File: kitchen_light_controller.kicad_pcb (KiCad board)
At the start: 2 copper layers, 48 x 57 mm, 10 parts, among them J1 1935161, J2 1935161, J3 1935161, U1 SC0915, U2 VND7140AJTR

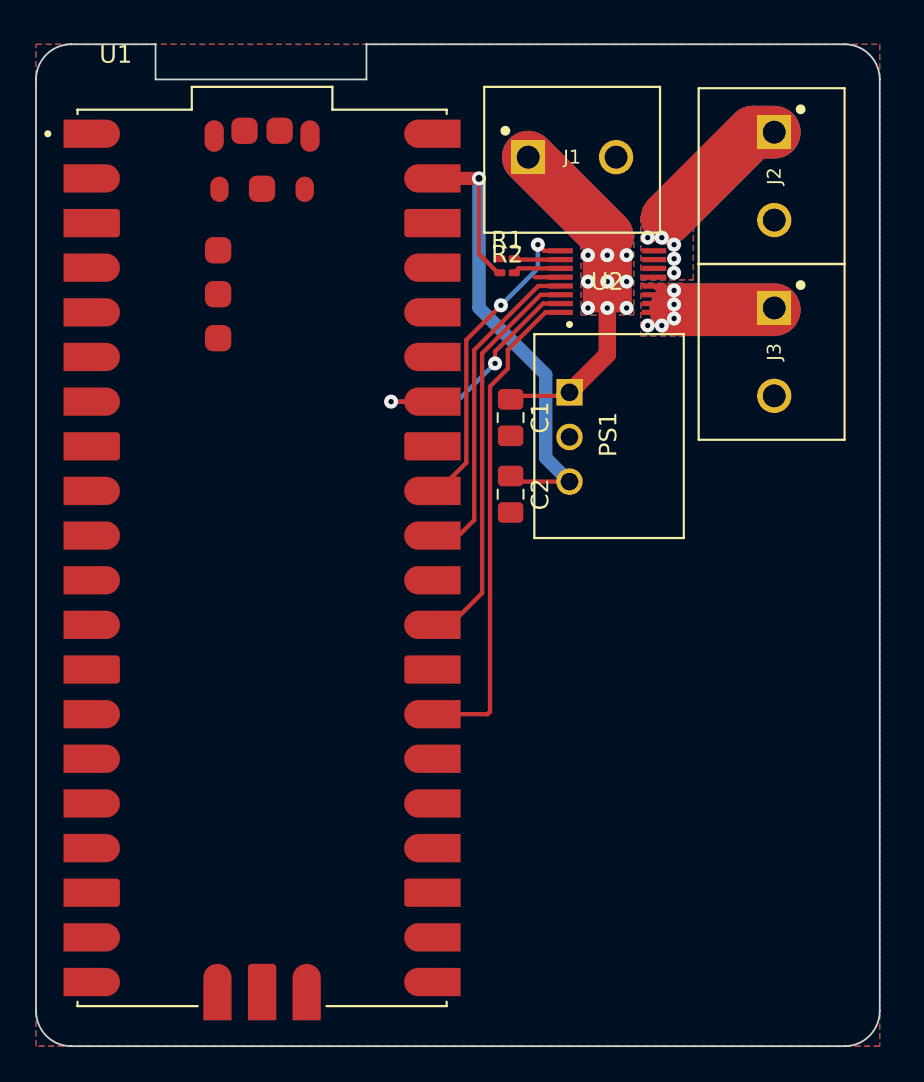
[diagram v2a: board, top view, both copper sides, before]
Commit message: Added debounced control switches
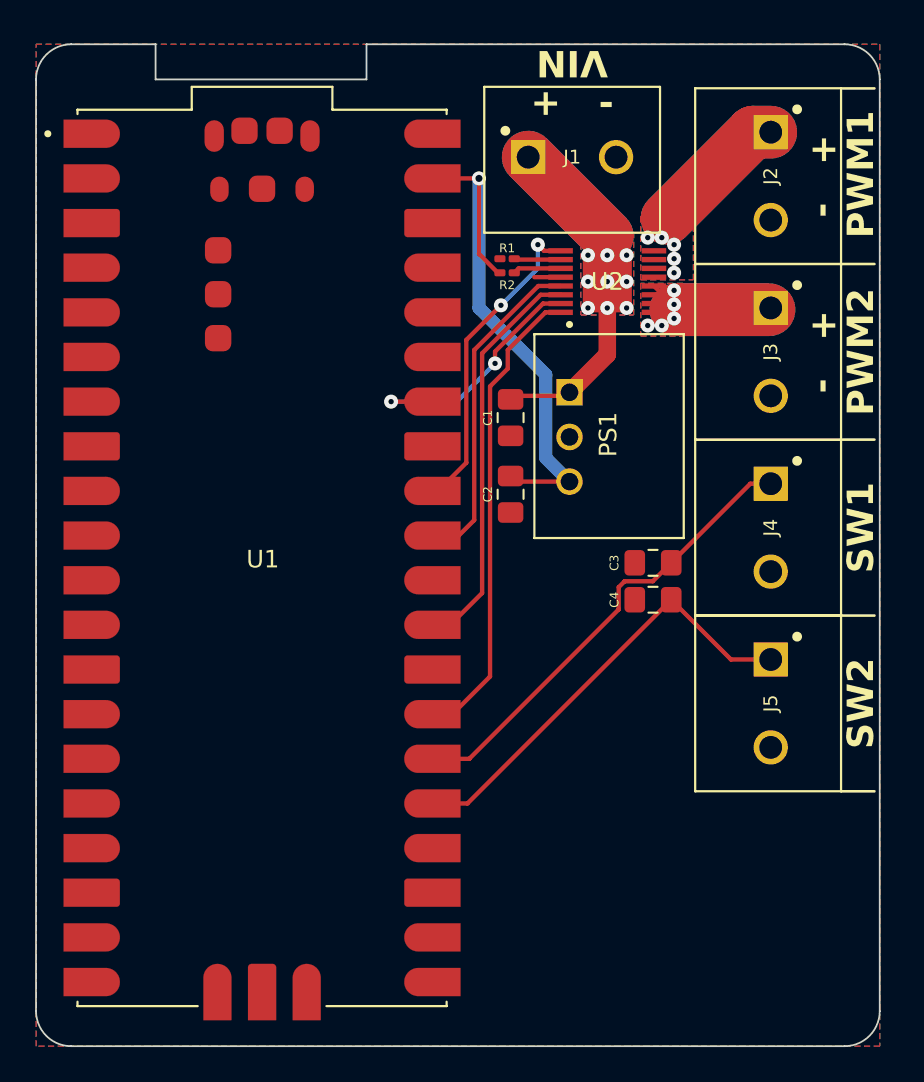
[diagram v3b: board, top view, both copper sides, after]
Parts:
- added C3: 1μF, Capacitor_SMD:C_0805_2012Metric_Pad1.18x1.45mm_HandSolder, F.Cu at (111.1, 58.5)
- added C4: 1μF, Capacitor_SMD:C_0805_2012Metric_Pad1.18x1.45mm_HandSolder, F.Cu at (111.1, 60.6)
- added J4: 1935161, Raspberry Pi Pico:PHOENIX_1935161, F.Cu at (117.8, 56.5)
- added J5: 1935161, Raspberry Pi Pico:PHOENIX_1935161, F.Cu at (117.8, 66.5)
- moved J2 0.20 mm to (117.8, 36.5)
- moved J3 0.20 mm to (117.8, 46.5)
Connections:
- U1 pad 13: Net-(U1-GND-Pad13) -> GND
- U1 pad 18: Net-(U1-GND-Pad13) -> GND
- U1 pad 23: Net-(U1-GND-Pad13) -> GND
- U1 pad 25: unconnected-(U1-GP19-Pad25) -> SW2
- U1 pad 26: unconnected-(U1-GP20-Pad26) -> SW1
- U1 pad 28: Net-(U1-GND-Pad13) -> GND
- U1 pad 3: Net-(U1-GND-Pad13) -> GND
- U1 pad 38: Net-(U1-GND-Pad13) -> GND
- U1 pad 8: Net-(U1-GND-Pad13) -> GND
- U1 pad D2: Net-(U1-GND-Pad13) -> GND
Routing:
- net SW1: track 0.00 -> 26.5 mm
- net SW2: track 0.00 -> 25.5 mm
- net 3.3V: track 34.1 -> 31.5 mm
- net PWM1: track 28.2 -> 27.1 mm
- net Net-(J3-Pad1): track 13.0 -> 12.4 mm
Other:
- board text added: "+ -"
- board text added: "PWM1"
- board text added: "PWM2"
- board text added: "SW1"
- board text added: "SW2"
- board text added: "VIN"

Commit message: Added analog motion sensor header
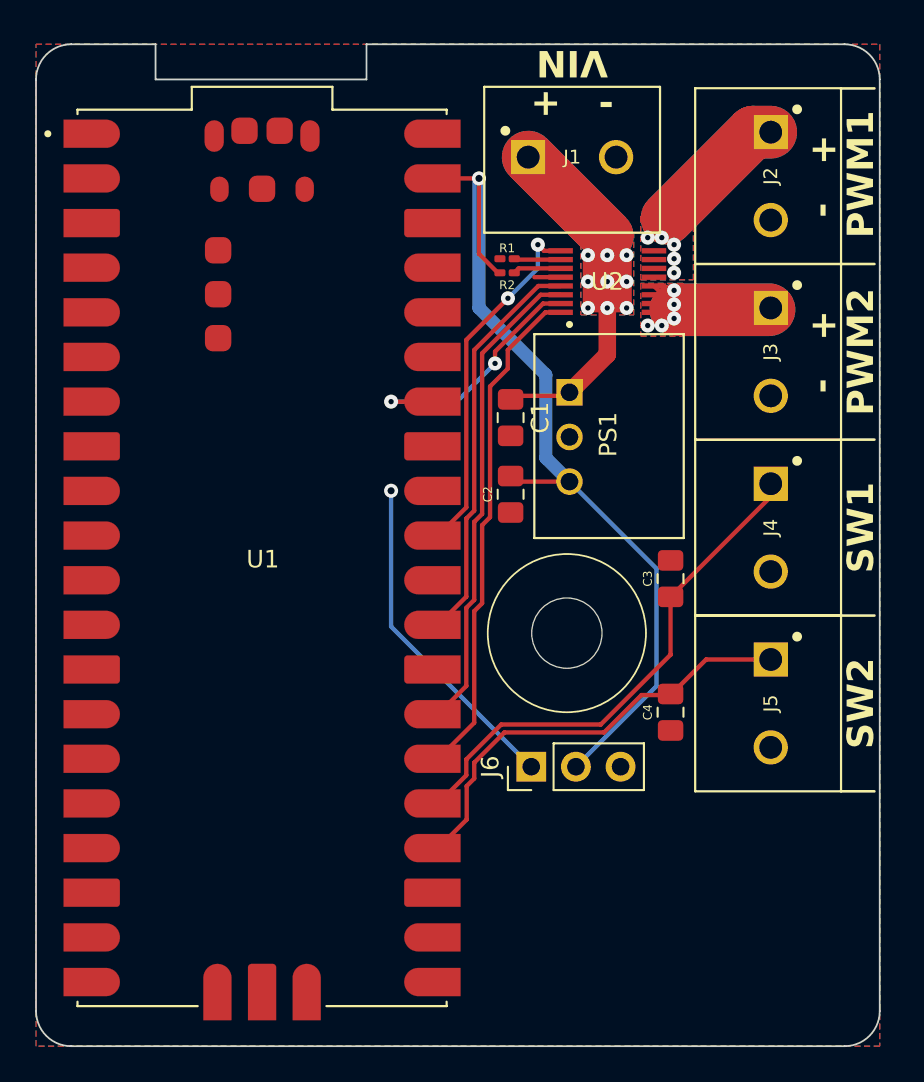
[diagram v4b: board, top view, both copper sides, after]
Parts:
- added J6: Conn_01x03, Connector_PinHeader_2.54mm:PinHeader_1x03_P2.54mm_Vertical, F.Cu at (104.2, 70.1)
- added REF**: MountingHole_Custom, kitchen_light_controller_parts:MountingHole_Custom, F.Cu at (106.2, 62.5)
- moved C4 6.48 mm to (112.1, 67.0), turned to 90 degrees
- moved C3 1.35 mm to (112.1, 59.4), turned to -90 degrees
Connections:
- U1 pad 24: unconnected-(U1-GP18-Pad24) -> SW2
- U1 pad 25: SW2 -> SW1
- U1 pad 26: SW1 -> PWM1
- U1 pad 27: PWM1 -> MS_SEL1
- U1 pad 29: MS_SEL1 -> MS_SEL0
- U1 pad 31: MS_SEL0 -> PWM0
- U1 pad 32: PWM0 -> MOTION_SIGNAL
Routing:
- net 3.3V: track 31.5 -> 51.7 mm
- net MOTION_SIGNAL: track 0.00 -> 19.3 mm, vias 0 -> 1
- net MS_SEL1: track 23.1 -> 28.9 mm
- net MS_SEL0: track 18.8 -> 23.8 mm
- net SW1: track 26.5 -> 29.7 mm
- net PWM0: track 18.1 -> 21.1 mm
- net PWM1: track 27.1 -> 29.1 mm

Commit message: Revision 1.0
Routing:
- net MOTION_SIGNAL: track 19.3 -> 21.7 mm
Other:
- board text added: "By Nicholas Hollander"
- board text added: "D V G"
- board text added: "INPUT 6-28V ≤12A"
- board text added: "PWM LED Driver v1.0"
